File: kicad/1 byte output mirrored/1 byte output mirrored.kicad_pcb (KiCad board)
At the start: 2 copper layers, 57.3 x 51.4 mm, 9 parts, among them J1 Conn_01x05_Male, J2 Conn_01x05_Female, J3 Conn_01x08, J4 Screw_Terminal_01x02, U1 74HCT595, U2 ULN2803A

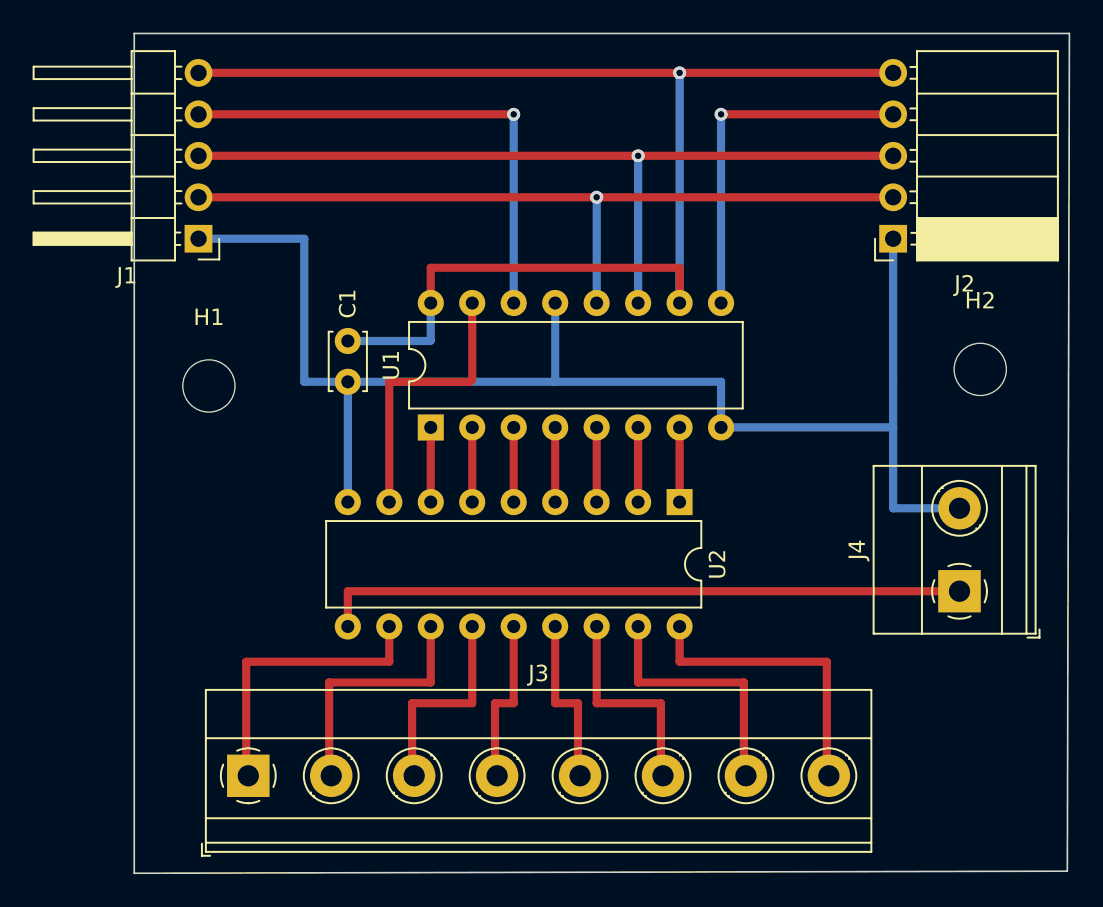
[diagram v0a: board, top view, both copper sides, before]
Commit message: added 2 byte mirrored output
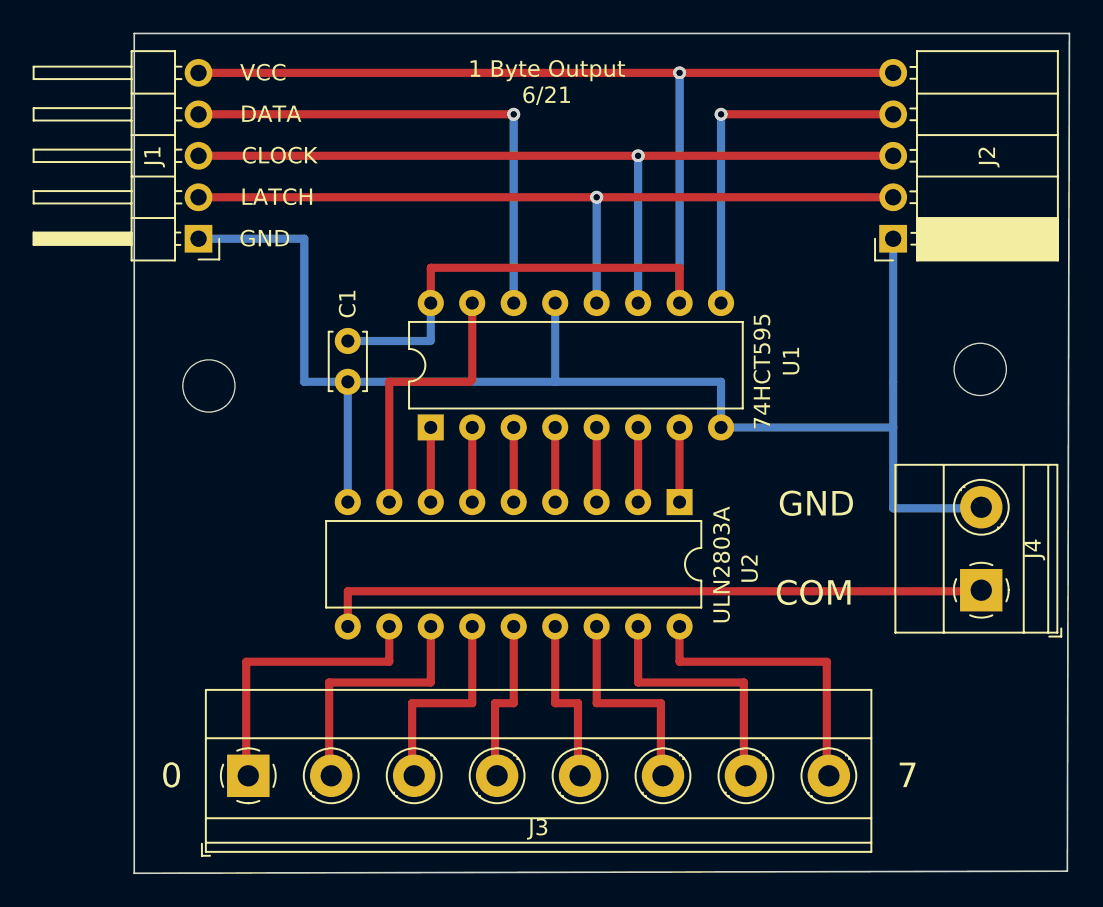
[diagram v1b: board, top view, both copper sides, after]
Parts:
-  : renamed from H2; value MountingHole -> (none)
-  : renamed from H1; value MountingHole -> (none)
- moved J4 1.34 mm to (166.3, 117.4)
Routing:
- net GND: track 86.9 -> 88.2 mm
- net COM: track 39.6 -> 41.0 mm
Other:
- board text added: "0"
- board text added: "1 Byte Output 6/21"
- board text added: "7"
- board text added: "CLOCK"
- board text added: "COM"
- board text added: "DATA"
- board text added: "GND"
- board text added: "LATCH"
- board text added: "VCC"
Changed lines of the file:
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@@
   (general
     (thickness 1.6)
-    (drawings 4)
-    (tracks 76)
+    (drawings 14)
+    (tracks 78)
     (zones 0)
     (modules 9)
@@
     (descr "Through hole angled pin header, 1x05, 2.54mm pitch, 6mm pin length, single row")
     (tags "Through hole angled pin header THT 1x05 2.54mm single row")
-    (fp_text reference J1 (at 4.385 -2.27) (layer F.SilkS)
+    (fp_text reference J1 (at 2.794 5.08 90) (layer F.SilkS)
       (effects (font (size 1 1) (thickness 0.15)))
     )
@@
     (tags "mounting hole 3.2mm no annular m3")
     (attr virtual)
-    (fp_text reference H2 (at 0 -4.2) (layer F.SilkS)
-      (effects (font (size 1 1) (thickness 0.15)))
-    )
-    (fp_text value MountingHole (at 0 4.2) (layer F.Fab)
+    (fp_text reference " " (at 0 -4.2) (layer F.SilkS) hide
+      (effects (font (size 1 1) (thickness 0.15)))
+    )
+    (fp_text value " " (at 0 4.2) (layer F.Fab) hide
       (effects (font (size 1 1) (thickness 0.15)))
     )
     (fp_circle (center 0 0) (end 3.2 0) (layer Cmts.User) (width 0.15))
     (fp_circle (center 0 0) (end 3.45 0) (layer F.CrtYd) (width 0.05))
-    (fp_text user %R (at 0.3 0) (layer F.Fab)
+    (fp_text user " " (at 0.3 0) (layer F.Fab) hide
       (effects (font (size 1 1) (thickness 0.15)))
     )
@@
     (tags "mounting hole 3.2mm no annular m3")
     (attr virtual)
-    (fp_text reference H1 (at 0 -4.2) (layer F.SilkS)
-      (effects (font (size 1 1) (thickness 0.15)))
-    )
-    (fp_text value MountingHole (at 0 4.2) (layer F.Fab)
+    (fp_text reference " " (at 0 -4.2) (layer F.SilkS) hide
+      (effects (font (size 1 1) (thickness 0.15)))
+    )
+    (fp_text value " " (at 0 4.2) (layer F.Fab) hide
       (effects (font (size 1 1) (thickness 0.15)))
     )
     (fp_circle (center 0 0) (end 3.2 0) (layer Cmts.User) (width 0.15))
     (fp_circle (center 0 0) (end 3.45 0) (layer F.CrtYd) (width 0.05))
-    (fp_text user %R (at 0.3 0) (layer F.Fab)
+    (fp_text user " " (at 0.3 0) (layer F.Fab) hide
       (effects (font (size 1 1) (thickness 0.15)))
     )
@@
     (descr "Through hole angled socket strip, 1x05, 2.54mm pitch, 8.51mm socket length, single row (from Kicad 4.0.7), script generated")
     (tags "Through hole angled socket strip THT 1x05 2.54mm single row")
-    (fp_text reference J2 (at -4.38 -2.77) (layer F.SilkS)
+    (fp_text reference J2 (at -5.7785 5.08 90) (layer F.SilkS)
       (effects (font (size 1 1) (thickness 0.15)))
     )
@@
     (descr "Terminal Block Phoenix MKDS-1,5-8-5.08, 8 pins, pitch 5.08mm, size 40.6x9.8mm^2, drill diamater 1.3mm, pad diameter 2.6mm, see http://www.farnell.com/datasheets/100425.pdf, script-generated using https://github.com/pointhi/kicad-footprint-generator/scripts/TerminalBlock_Phoenix")
     (tags "THT Terminal Block Phoenix MKDS-1,5-8-5.08 pitch 5.08mm size 40.6x9.8mm^2 drill 1.3mm pad 2.6mm")
-    (fp_text reference J3 (at 17.78 -6.26) (layer F.SilkS)
+    (fp_text reference J3 (at 17.78 3.175) (layer F.SilkS)
       (effects (font (size 1 1) (thickness 0.15)))
     )
@@
   )
   (module TerminalBlock_Phoenix:TerminalBlock_Phoenix_MKDS-1,5-2-5.08_1x02_P5.08mm_Horizontal (layer F.Cu)
-    (at 164.973 117.475 90)
+    (at 166.3065 117.4115 90)
     (descr "Terminal Block Phoenix MKDS-1,5-2-5.08, 2 pins, pitch 5.08mm, size 10.2x9.8mm^2, drill diamater 1.3mm, pad diameter 2.6mm, see http://www.farnell.com/datasheets/100425.pdf, script-generated using https://github.com/pointhi/kicad-footprint-generator/scripts/TerminalBlock_Phoenix")
     (tags "THT Terminal Block Phoenix MKDS-1,5-2-5.08 pitch 5.08mm size 10.2x9.8mm^2 drill 1.3mm pad 2.6mm")
-    (fp_text reference J4 (at 2.54 -6.26 90) (layer F.SilkS)
+    (fp_text reference J4 (at 2.54 3.175 90) (layer F.SilkS)
       (effects (font (size 1 1) (thickness 0.15)))
     )
@@
     (descr "16-lead though-hole mounted DIP package, row spacing 7.62 mm (300 mils)")
     (tags "THT DIP DIL PDIP 2.54mm 7.62mm 300mil")
-    (fp_text reference U1 (at 3.81 -2.413 90) (layer F.SilkS)
-      (effects (font (size 1 1) (thickness 0.15)))
-    )
-    (fp_text value 74HCT595 (at 3.81 20.11 90) (layer F.Fab)
+    (fp_text reference U1 (at 4.064 22.098 90) (layer F.SilkS)
+      (effects (font (size 1 1) (thickness 0.15)))
+    )
+    (fp_text value 74HCT595 (at 3.429 20.32 90) (layer F.SilkS)
       (effects (font (size 1 1) (thickness 0.15)))
     )
@@
     (descr "18-lead though-hole mounted DIP package, row spacing 7.62 mm (300 mils)")
     (tags "THT DIP DIL PDIP 2.54mm 7.62mm 300mil")
-    (fp_text reference U2 (at 3.81 -2.33 90) (layer F.SilkS)
-      (effects (font (size 1 1) (thickness 0.15)))
-    )
-    (fp_text value ULN2803A (at 3.81 22.65 90) (layer F.Fab)
+    (fp_text reference U2 (at 4.064 -4.318 90) (layer F.SilkS)
+      (effects (font (size 1 1) (thickness 0.15)))
+    )
+    (fp_text value ULN2803A (at 3.8735 -2.6035 90) (layer F.SilkS)
       (effects (font (size 1 1) (thickness 0.15)))
     )
@@
     )
   )
+  (gr_text "1 Byte Output\n6/21" (at 139.7 86.2965) (layer F.SilkS)
+    (effects (font (size 1 1) (thickness 0.15)))
+  )
+  (gr_text GND (at 122.428 95.885) (layer F.SilkS)
+    (effects (font (size 1 1) (thickness 0.15)))
+  )
+  (gr_text LATCH (at 123.19 93.345) (layer F.SilkS)
+    (effects (font (size 1 1) (thickness 0.15)))
+  )
+  (gr_text CLOCK (at 123.317 90.805) (layer F.SilkS)
+    (effects (font (size 1 1) (thickness 0.15)))
+  )
+  (gr_text DATA (at 120.904 88.265) (layer F.SilkS)
+    (effects (font (size 1 1) (thickness 0.15)) (justify left))
+  )
+  (gr_text VCC (at 120.904 85.725) (layer F.SilkS)
+    (effects (font (size 1 1) (thickness 0.15)) (justify left))
+  )
+  (gr_text 7 (at 161.798 128.778) (layer F.SilkS)
+    (effects (font (size 1.5 1.5) (thickness 0.3)))
+  )
+  (gr_text 0 (at 116.713 128.778) (layer F.SilkS)
+    (effects (font (size 1.5 1.5) (thickness 0.3)))
+  )
+  (gr_text COM (at 156.083 117.602) (layer F.SilkS)
+    (effects (font (size 1.5 1.5) (thickness 0.3)))
+  )
+  (gr_text GND (at 156.21 112.141) (layer F.SilkS)
+    (effects (font (size 1.5 1.5) (thickness 0.3)))
+  )
   (gr_line (start 114.427 134.747) (end 114.427 83.312) (layer Edge.Cuts) (width 0.1))
   (gr_line (start 171.577 134.62) (end 114.427 134.747) (layer Edge.Cuts) (width 0.1))
@@
   (segment (start 150.368 104.648) (end 140.208 104.648) (width 0.5) (layer B.Cu) (net 1))
   (segment (start 160.909 104.648) (end 160.909 95.885) (width 0.5) (layer B.Cu) (net 1))
-  (segment (start 160.909 112.395) (end 164.973 112.395) (width 0.5) (layer B.Cu) (net 1))
   (segment (start 150.368 107.442) (end 160.909 107.442) (width 0.5) (layer B.Cu) (net 1))
   (segment (start 160.909 107.442) (end 160.909 112.395) (width 0.5) (layer B.Cu) (net 1))
@@
   (segment (start 124.841 104.648) (end 124.841 95.885) (width 0.5) (layer B.Cu) (net 1))
   (segment (start 124.841 95.885) (end 118.364 95.885) (width 0.5) (layer B.Cu) (net 1))
+  (segment (start 166.243 112.395) (end 166.3065 112.3315) (width 0.5) (layer B.Cu) (net 1))
+  (segment (start 160.909 112.395) (end 166.243 112.395) (width 0.5) (layer B.Cu) (net 1))
   (segment (start 118.364 93.345) (end 160.909 93.345) (width 0.5) (layer F.Cu) (net 2))
   (segment (start 142.748 99.822) (end 142.748 93.345) (width 0.5) (layer B.Cu) (net 2))
@@
   (segment (start 121.285 121.793) (end 121.285 128.778) (width 0.5) (layer F.Cu) (net 14))
   (segment (start 127.508 119.634) (end 127.508 117.475) (width 0.5) (layer F.Cu) (net 15))
-  (segment (start 127.508 117.475) (end 164.973 117.475) (width 0.5) (layer F.Cu) (net 15))
+  (segment (start 166.243 117.475) (end 166.3065 117.4115) (width 0.5) (layer F.Cu) (net 15))
+  (segment (start 127.508 117.475) (end 166.243 117.475) (width 0.5) (layer F.Cu) (net 15))
   (segment (start 132.588 107.442) (end 132.588 112.014) (width 0.5) (layer F.Cu) (net 16))
   (segment (start 135.128 107.442) (end 135.128 112.014) (width 0.5) (layer F.Cu) (net 17))

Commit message: added dcc sniffer, conversion to kicad 6
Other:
- net class Default removed
